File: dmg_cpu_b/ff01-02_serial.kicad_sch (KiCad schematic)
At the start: 64 parts

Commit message: First lot of fixes based on issues found.
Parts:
- SCK: value IOBUF_B -> IOBUF_C; symbol DMG_CPU_Cells:IOBUF_B -> DMG_CPU_Cells:IOBUF_C
- gave numbers to parts that had none: 1
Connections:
- net GND is gone; now on net SCK_DIR: SCK.3 (~{ENA}_PU)
- net at KUJO.3: now also SCK.1 (DRV_LOW); no longer SCK.4 (~{DRV}_HIGH)
- net at KEXU.3: now also SCK.4 (~{DRV}_HIGH); no longer SCK.1 (DRV_LOW)
- net SIN renamed ~{SIN}
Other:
- moved on the sheet: CAVE, COTY, DAWA, JAGO, KEXU, KUJO, SCK

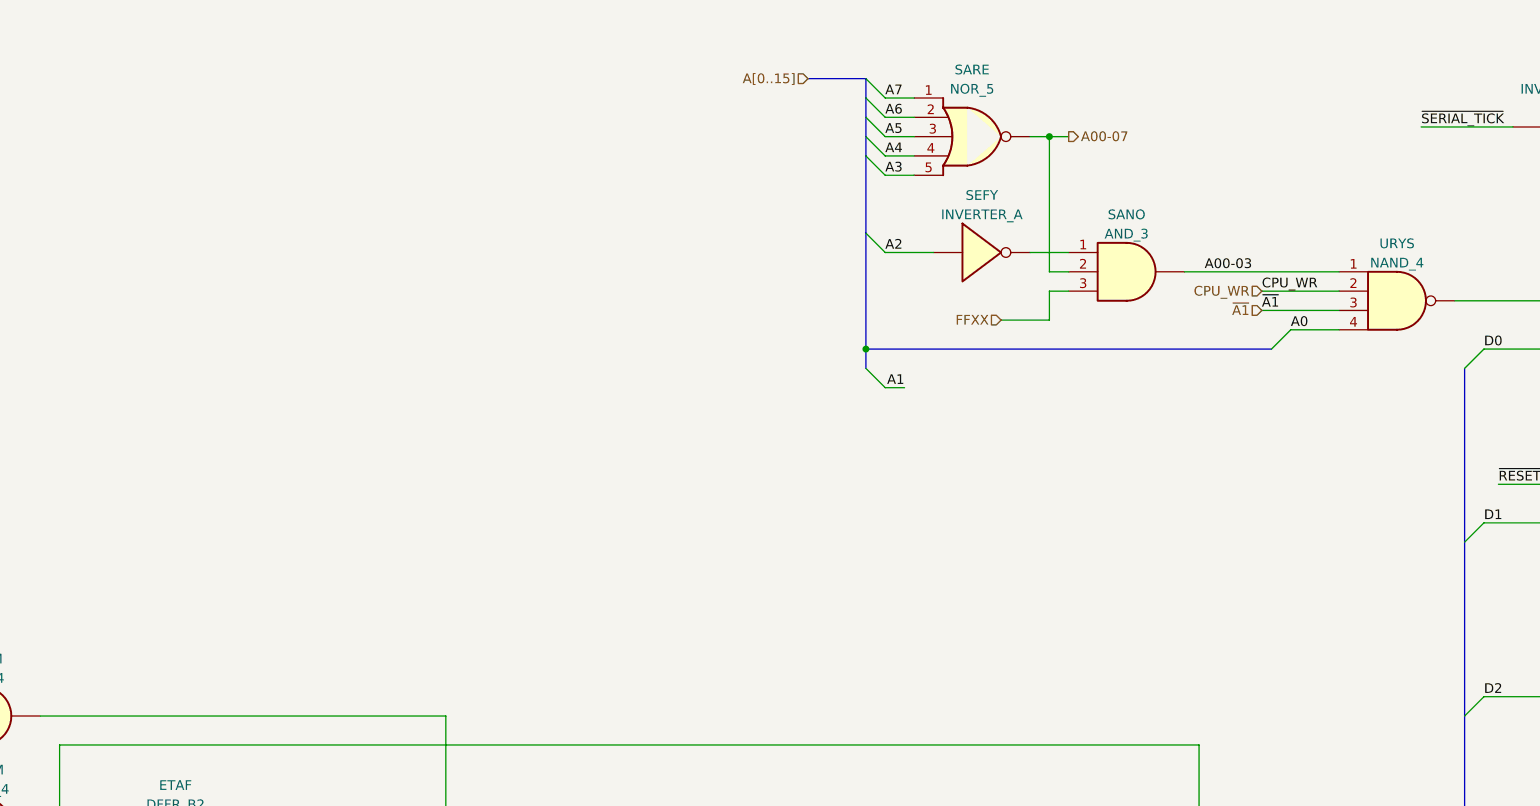
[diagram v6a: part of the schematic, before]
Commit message: New sheet created to free up space on LCD and SCX/SCY sheets and joined common signals.
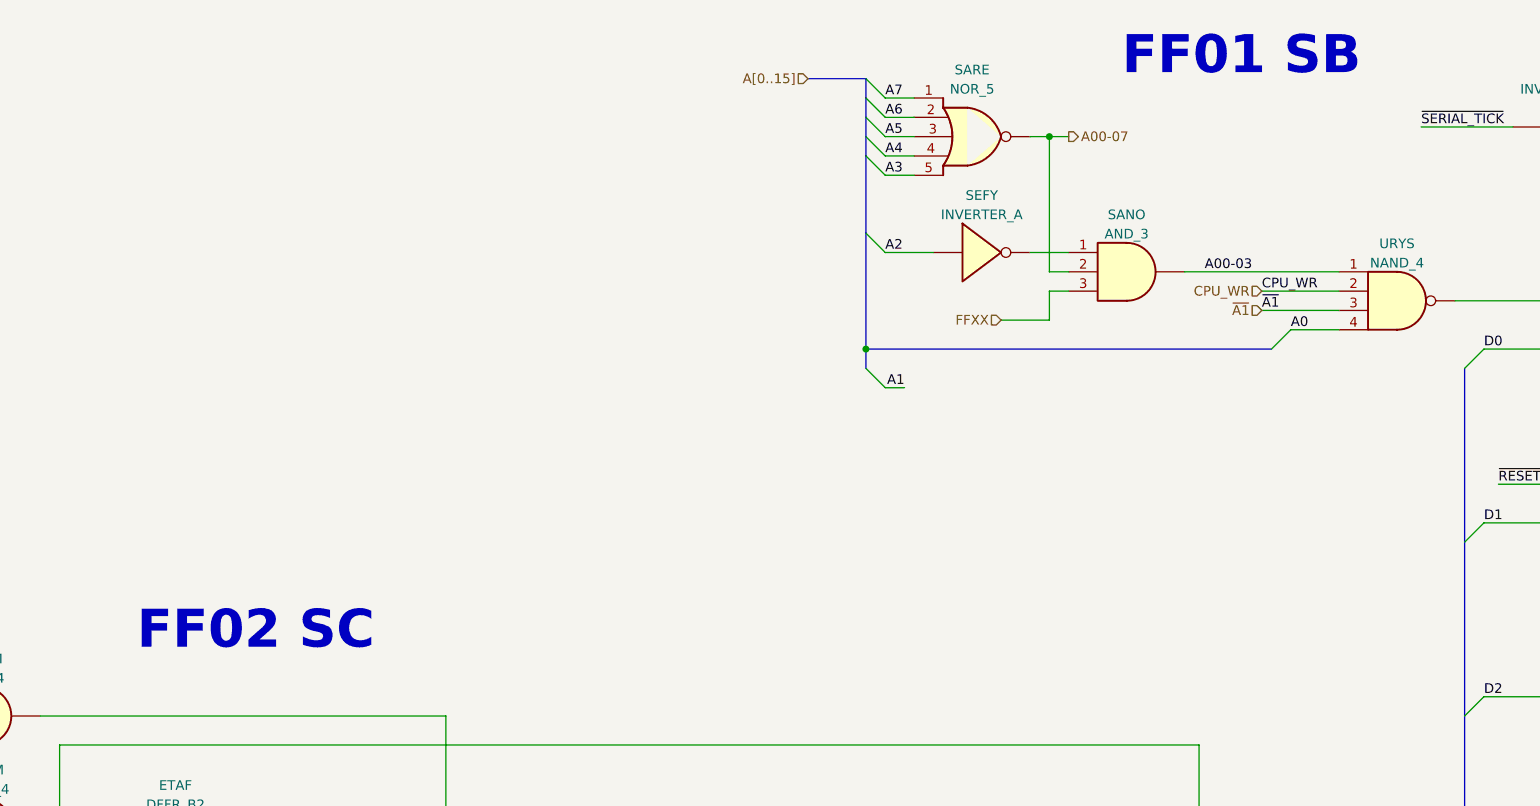
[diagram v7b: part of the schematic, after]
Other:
- note added: "FF01 SB"
- note added: "FF02 SC"
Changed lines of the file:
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@@
     (stroke (width 0) (type default) (color 0 0 0 0))
+  )
+  (text "FF02 SC\n" (at 67.945 102.87 0)
+    (effects (font (size 5 5) (thickness 1) bold) (justify left bottom))
+  )
+  (text "FF01 SB\n" (at 197.485 27.305 0)
+    (effects (font (size 5 5) (thickness 1) bold) (justify left bottom))
   )
   (label "CPU_RD" (at 20.955 109.855 0)
